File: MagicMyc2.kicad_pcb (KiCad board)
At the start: 2 copper layers, 43 x 31 mm, 32 parts, among them J1 RGB, J2 SPI, J3 PowerSupply, J4 Aout, J5 GPIOs, J6 PRG, J8 10102166A812A, Q1 BC338, U1 PIC18F15Q41-I/SS, U3 NCP1117-3.3_SOT223

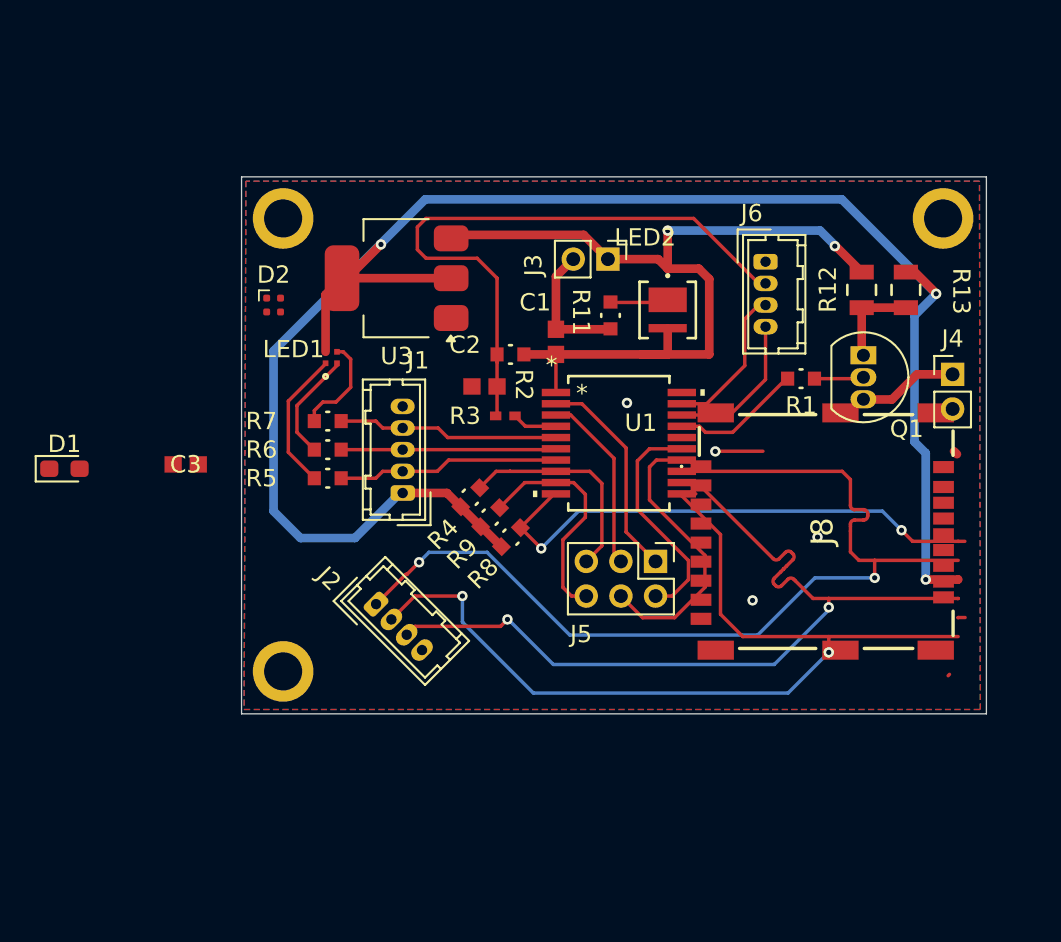
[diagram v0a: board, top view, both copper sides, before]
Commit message: v2: changed Pinout, Layout; removed 6V PG-LED
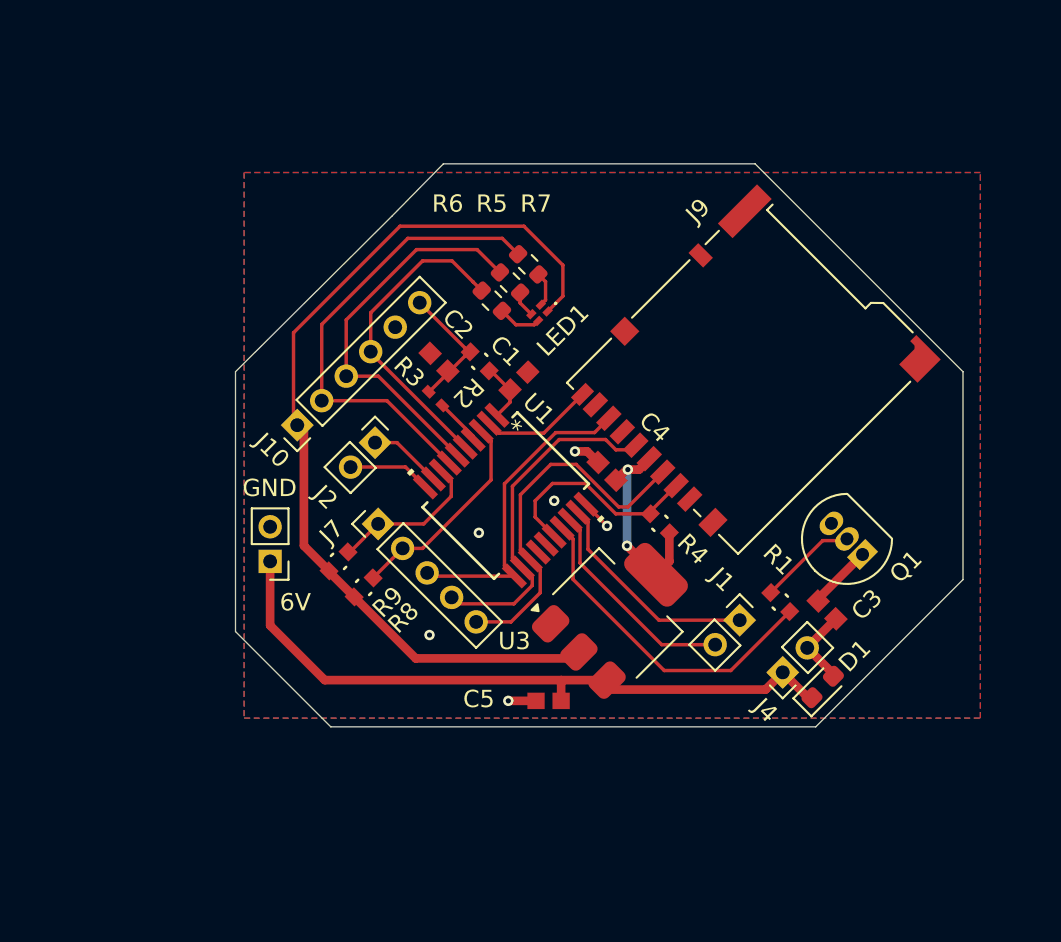
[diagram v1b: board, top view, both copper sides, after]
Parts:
- removed D2: ASMB-MTB1-0A3A2, LED_SMD:LED_Wurth_150044M155260
- removed J5: GPIOs, Connector_PinHeader_2.00mm:PinHeader_2x03_P2.00mm_Vertical
- removed J6: PRG, Connector_Hirose:Hirose_DF13-04P-1.25DSA_1x04_P1.25mm_Vertical
- removed J8: 10102166A812A, 10102166A812A:10102166A812A
- removed LED2: PG_6V, JB3030AWT-P-B65EA0000-N0000001:LED_J-SERIES_3030_CRW
- removed R11: 51 Ohm, RT0603DRE0710KL:RC0603N_YAG
- removed R12, R13: 0 Ohm, CRCW08050000Z0EA:RES_CRCW_0805_VIS
- removed REF** (x3): MountingHole_2.2mm_M2_ISO7380_Pad, MountingHole:MountingHole_2.2mm_M2_ISO7380_Pad
- added C4: 0.1 uF, C0603C103M5RAC7411:CAPC17595_87N_KEM, F.Cu at (76.0, 74.8)
- added C5: ? uF, C0603C103M5RAC7411:CAPC17595_87N_KEM, F.Cu at (72.6, 88.0)
- added J10: Conn_01x06, Connector_PinHeader_2.00mm:PinHeader_1x06_P2.00mm_Vertical, F.Cu at (58.1, 72.1)
- added J7: SPI_out, Connector_PinHeader_2.00mm:PinHeader_1x05_P2.00mm_Vertical, F.Cu at (62.7, 77.8)
- added J9: DM3BT-DSF-PEJS, Connector_Card:microSD_HC_Hirose_DM3BT-DSF-PEJS, F.Cu at (84.2, 69.0)
- J1: value RGB -> PowerSupply; footprint Connector_Hirose:Hirose_DF13-05P-1.25DSA_1x05_P1.25mm_Vertical -> Connector_PinHeader_2.00mm:PinHeader_1x02_P2.00mm_Vertical
- J2: value SPI -> PowerSupply; footprint Connector_Hirose:Hirose_DF13-04P-1.25DSA_1x04_P1.25mm_Vertical -> Connector_PinHeader_2.00mm:PinHeader_1x02_P2.00mm_Vertical
- LED1: value LED_RGB -> ASCB-HTC2-0A309; footprint UHD111A-FKA-C3K23E1L3VG5ZB3Z3:SMD4_UHD111A-FKA_CRW -> ASCB-HTC2-0A309:ASCBHTC20A309
- R5, R6, R7: value 51 Ohm -> 130; footprint RT0603DRE0710KL:RC0603N_YAG -> Resistor_SMD:R_0603_1608Metric
- moved D1 45.6 mm to (88.4, 87.2), turned to 45 degrees
- moved C3 38.0 mm to (88.7, 82.8), turned to 135 degrees
- moved J3 26.2 mm to (56.5, 80.0), turned to 180 degrees
- moved U3 23.2 mm to (76.5, 83.0), turned to 45 degrees
- moved J1 20.8 mm to (83.6, 83.3), turned to -45 degrees
- moved J4 19.8 mm to (86.1, 86.4), turned to 135 degrees
- moved R5 15.4 mm to (70.3, 63.9), turned to -45 degrees
- moved R7 14.7 mm to (71.4, 62.8), turned to 135 degrees
- moved R1 13.0 mm to (86.0, 82.3), turned to 135 degrees
- moved R6 12.8 mm to (69.3, 64.9), turned to 135 degrees
- moved LED1 12.3 mm to (72.0, 65.6), turned to 45 degrees
- moved Q1 11.5 mm to (90.7, 79.5), turned to 135 degrees
- moved R4 11.1 mm to (79.0, 77.8), turned to 135 degrees
- moved J2 9.32 mm to (62.6, 73.1)
- moved R9 9.12 mm to (60.5, 80.0)
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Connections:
- J1 pad 1: 3.3V -> ICSP_DATA
- J1 pad 2: LED_B -> ICSP_CLK
- J2 pad 1: SPI_MOSI -> RC7
- J2 pad 2: SPI_MISO -> RB7
- J4 pad 1: Aout -> Speaker_out
- J4 pad 2: GND -> Speaker_in 
- LED1 pad 1: Net-(LED1-Pad1) -> 3.3V
- LED1 pad 2: Net-(LED1-Pad2) -> Net-(LED1-CATHODE_BLUE)
- LED1 pad 3: Net-(LED1-Pad3) -> Net-(LED1-CATHODE_GREEN)
- LED1 pad 4: 3.3V -> Net-(LED1-CATHODE_RED)
- R4 pad 2: SPI_nCS3 -> SPI_nCS1
- R5 pad 1: unconnected-(R5-Pad1) -> LED_G
- R5 pad 2: LED_B -> Net-(LED1-CATHODE_GREEN)
- R6 pad 1: unconnected-(R6-Pad1) -> Net-(LED1-CATHODE_RED)
- R6 pad 2: LED_G -> LED_R
- R7 pad 1: LED_R -> Net-(LED1-CATHODE_BLUE)
- R7 pad 2: unconnected-(R7-Pad2) -> LED_B
- R8 pad 2: SPI_nCS1 -> SPI_nCS3
- U1 pad 10: SPI_nCS1 -> RB7
- U1 pad 16: unconnected-(U1-RC0-Pad16) -> SPI_nCS1
- U1 pad 2: RA5 -> SD_DETECT
- U1 pad 3: RA4 -> SPI_nCS3
- U1 pad 8: SPI_nCS3 -> SPI_nCS2
- U1 pad 9: SPI_nCS2 -> RC7
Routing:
- net VCC 6V: track 51.0 -> 0.00 mm
- net 3.3V: track 105.0 -> 65.4 mm, vias 3 -> 2
- net Speaker_out: track 0.00 -> 39.0 mm
- net SPI_MISO: track 53.8 -> 18.3 mm, vias 2 -> 0
- net SPI_MOSI: track 56.5 -> 21.3 mm, vias 2 -> 0
- net SPI_SCK: track 49.8 -> 20.0 mm, vias 2 -> 0
- net MCLR: track 36.7 -> 7.20 mm
- net SPI_nCS1: track 31.2 -> 12.5 mm, vias 2 -> 0
- net RC2: track 16.4 -> 0.00 mm
- net LED_B: track 12.8 -> 27.2 mm
- net RC1: track 13.2 -> 0.00 mm
- net RA5: track 12.4 -> 0.00 mm
- net DAC: track 7.49 -> 19.3 mm
- net RA4: track 10.5 -> 0.00 mm
- net LED_G: track 12.5 -> 22.8 mm
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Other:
- board size 43 x 31 mm -> 42 x 32.5 mm
- board text added: "6V"
- board text added: "GND"

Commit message: added drill holes back
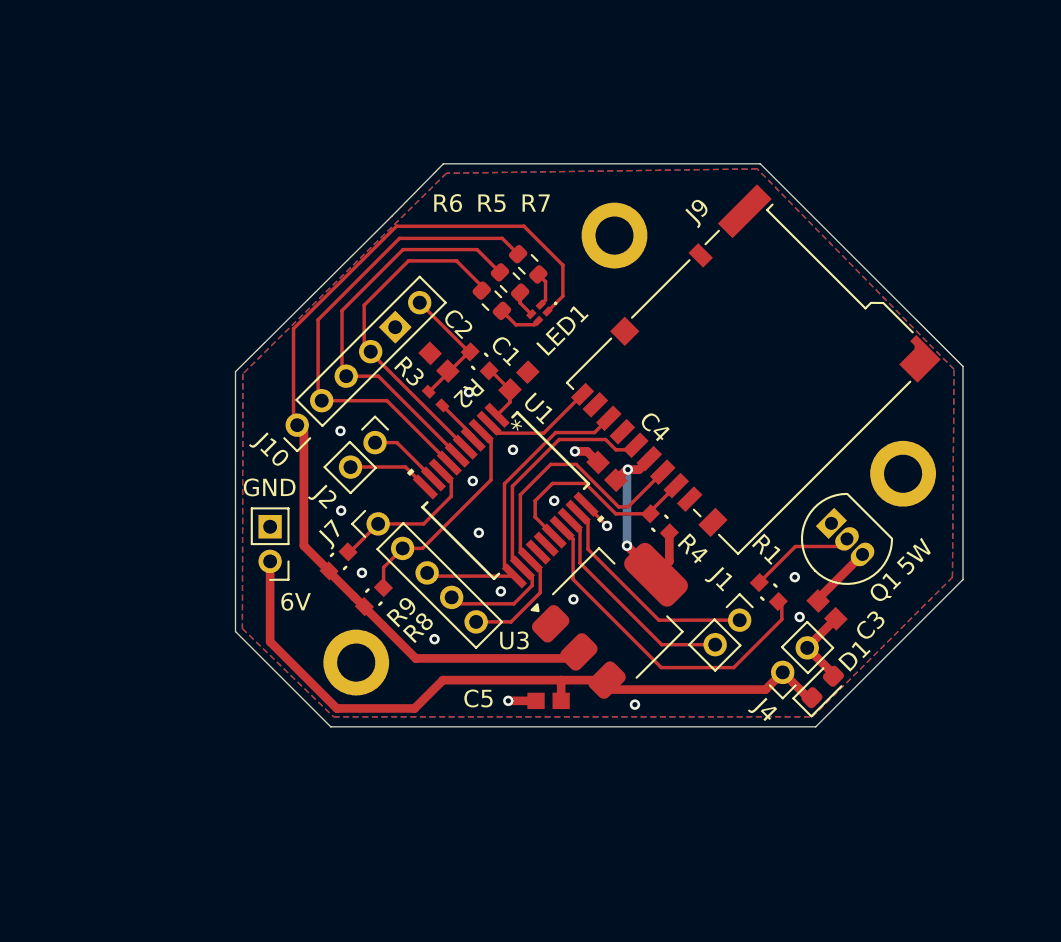
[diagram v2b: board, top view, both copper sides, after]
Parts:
- added REF**: MountingHole_2.2mm_M2_DIN965_Pad, MountingHole:MountingHole_2.2mm_M2_DIN965_Pad, F.Cu at (76.4, 61.1)
- added REF**: MountingHole_2.2mm_M2_DIN965_Pad, MountingHole:MountingHole_2.2mm_M2_DIN965_Pad, F.Cu at (93.0, 74.9)
- added REF**: MountingHole_2.2mm_M2_DIN965_Pad, MountingHole:MountingHole_2.2mm_M2_DIN965_Pad, F.Cu at (61.5, 85.8)
- moved R1 0.88 mm to (85.3, 81.7)
- moved R8 0.81 mm to (62.5, 82.0)
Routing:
- net Speaker_out: track 39.0 -> 40.9 mm
- net LED_R: track 18.4 -> 19.4 mm
- net LED_G: track 22.8 -> 23.4 mm
- net GND: track 4.95 -> 5.46 mm, vias 6 -> 17
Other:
- outline, holes or cut-outs redrawn
- board text added: "5W"

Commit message: Updated schematic pdf + some 3D models
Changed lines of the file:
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@@
 		(tags "CMS SOT")
 		(property "Reference" "U3"
-			(at -5.338656 -3.075914 0)
+			(at -5.444722 -3.082986 0)
 			(layer "F.SilkS")
 			(effects
@@
 			)
 		)
-		(model "S:/KiCad/Downloads/LIB_DM3BT-DSF-PEJS/DM3BT-DSF-PEJS/3D/DM3BT-DSF-PEJS.stl"
+		(model "${KICAD8_3DMODEL_DIR}/Connector_Card.3dshapes/microSD_HC_Hirose_DM3AT-SF-PEJM5.step"
 			(offset
 				(xyz 0 0 0)
@@
 		(tags "C0603C103M5RAC7411 ")
 		(property "Reference" "C2"
-			(at 0.777817 2.333452 -45)
+			(at 0.799031 2.411234 -45)
 			(unlocked yes)
 			(layer "F.SilkS")
@@
 		(tags "Through hole pin header THT 1x06 2.00mm single row")
 		(property "Reference" "J10"
-			(at 0 -2.06 135)
+			(at 0 -2.2832 135)
 			(layer "F.SilkS")
 			(effects
@@
 		(tags "Through hole pin header THT 1x02 2.00mm single row")
 		(property "Reference" "J4"
-			(at -0.848528 -2.252691 135)
+			(at -0.403051 -2.429468 0)
 			(layer "F.SilkS")
 			(effects
@@
 		(tags "LED")
 		(property "Reference" "LED1"
-			(at 0.247488 1.661702 45)
+			(at 0.98995 1.569778 -135)
 			(layer "F.SilkS")
 			(effects
@@
 		(tags "C0603C103M5RAC7411 ")
 		(property "Reference" "C1"
-			(at -0.689214 1.767767 -45)
+			(at -0.887204 1.45664 45)
 			(unlocked yes)
 			(layer "F.SilkS")
@@
 			)
 		)
+		(model "${KICAD8_3DMODEL_DIR}/Capacitor_SMD.3dshapes/C_01005_0402Metric.step"
+			(offset
+				(xyz 0 0 0)
+			)
+			(scale
+				(xyz 5 4 3)
+			)
+			(rotate
+				(xyz 0 0 0)
+			)
+		)
 	)
 	(footprint "Connector_PinHeader_2.00mm:PinHeader_1x02_P2.00mm_Vertical"
@@
 		(tags "to-92 sc-43 sc-43a sot54 PA33 transistor")
 		(property "Reference" "Q1"
-			(at -2.269813 -0.417193 45)
+			(at -2.2486 0.919239 45)
 			(layer "F.SilkS")
 			(effects
@@
 		(fp_arc
 			(start 0.3048 -3.7465)
-			(mid 0 -3.441698)
+			(mid 0 -3.441697)
 			(end -0.3048 -3.7465)
 			(stroke
@@
 			(font
 				(size 1 1)
-				(thickness 0.1)
+				(thickness 0.2)
+				(bold yes)
 			)
 			(justify left bottom)
@@
 	)
 	(gr_text "5W"
-		(at 94.15 80.13 45)
+		(at 93.93 78.61 0)
 		(layer "F.SilkS")
 		(effects
@@
 			(font
 				(size 1 1)
-				(thickness 0.1)
+				(thickness 0.2)
+				(bold yes)
 			)
 			(justify left bottom)

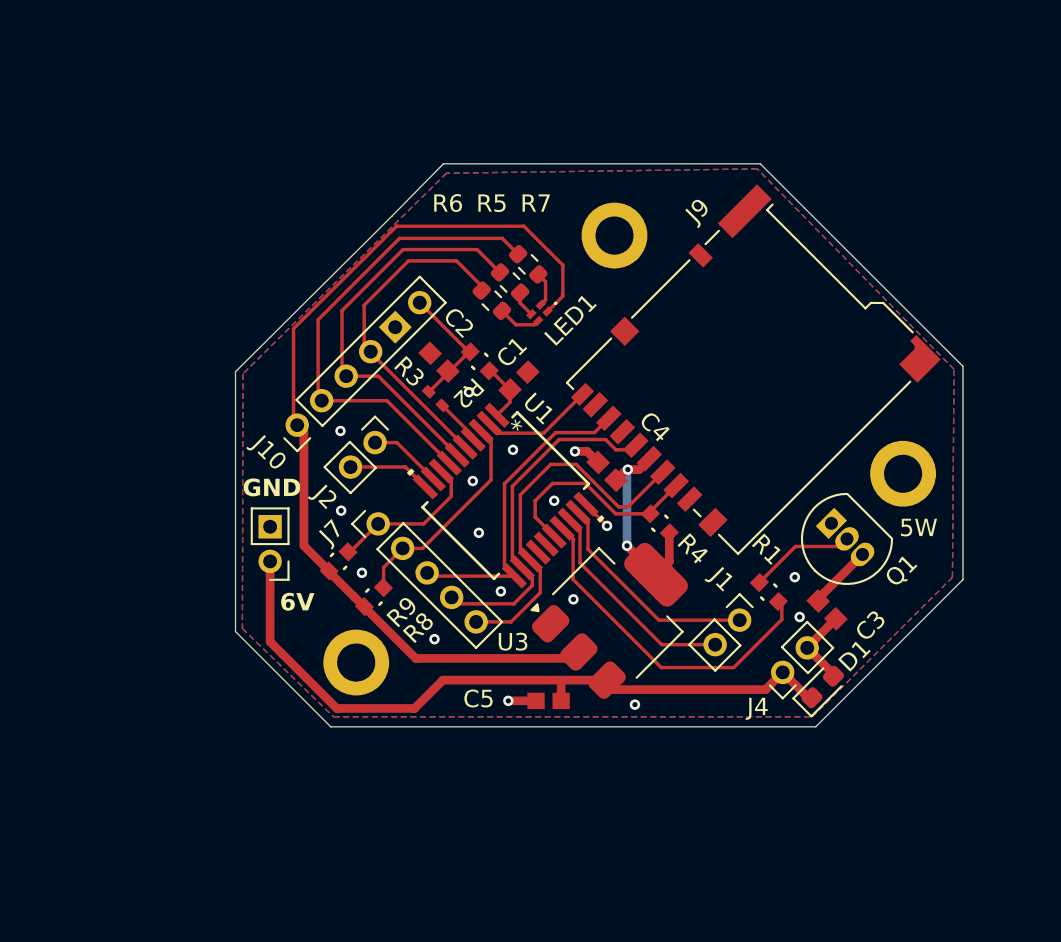
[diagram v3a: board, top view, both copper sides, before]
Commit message: Added design optimizations + Removed little ground islands by increasing min area size + Added teardrops + Fixes (almost) all errors + Added another 130Ohm resistor for RGB-LED (green) to maximize green power
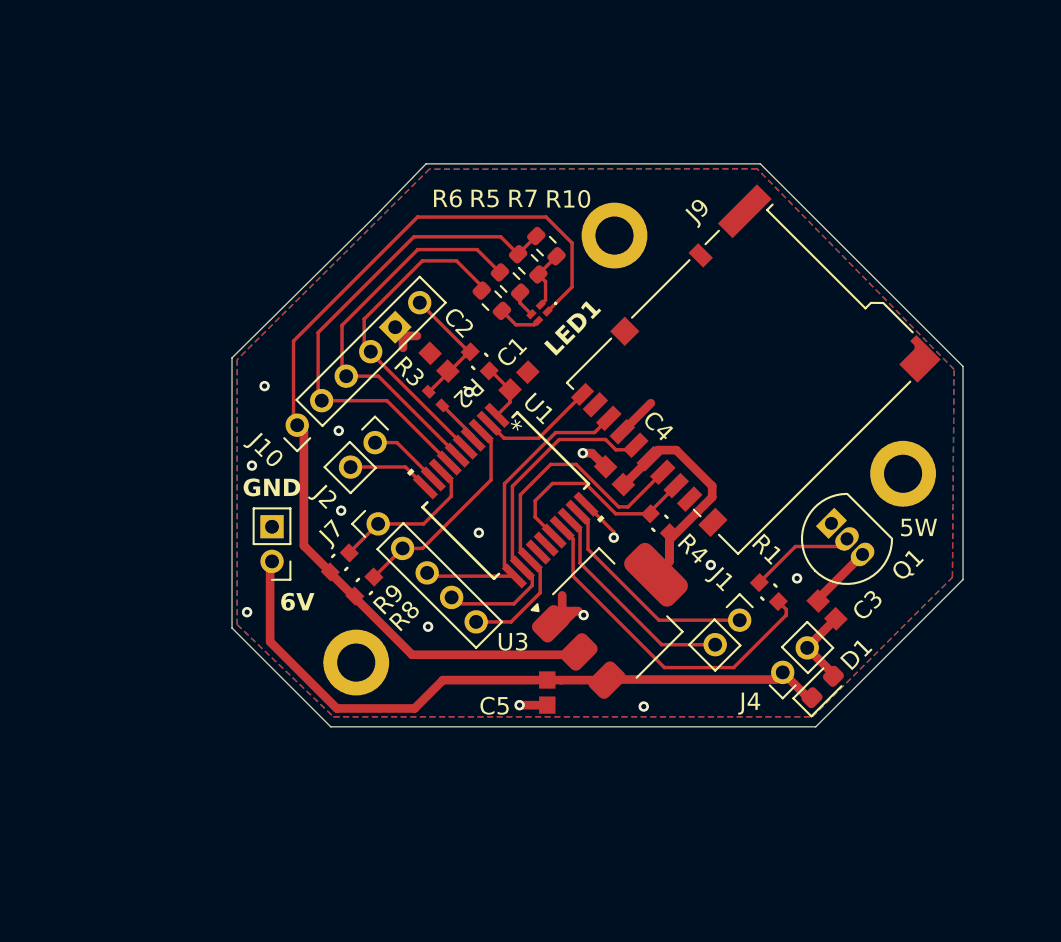
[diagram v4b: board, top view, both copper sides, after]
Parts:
- added R10: 130, Resistor_SMD:R_0603_1608Metric, F.Cu at (72.5, 61.8)
- moved R8 0.82 mm to (61.9, 81.4)
- moved C4 0.50 mm to (76.4, 75.0)
- moved C5 0.49 mm to (72.5, 87.5), turned to -90 degrees
- moved J3 0.11 mm to (56.6, 80.0)
- moved R9 0.09 mm to (60.5, 80.0)
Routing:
- net GND: track 5.46 -> 16.5 mm, vias 17 -> 15
- net 3.3V: track 65.6 -> 69.8 mm, vias 2 -> 0
- net Net-(LED1-CATHODE_BLUE): track 2.03 -> 3.52 mm
- net LED_B: track 27.7 -> 28.8 mm
- net Speaker_out: track 40.9 -> 39.8 mm
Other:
- board size 42 x 32.5 mm -> 42.2 x 32.5 mm

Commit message: Added rounded corners
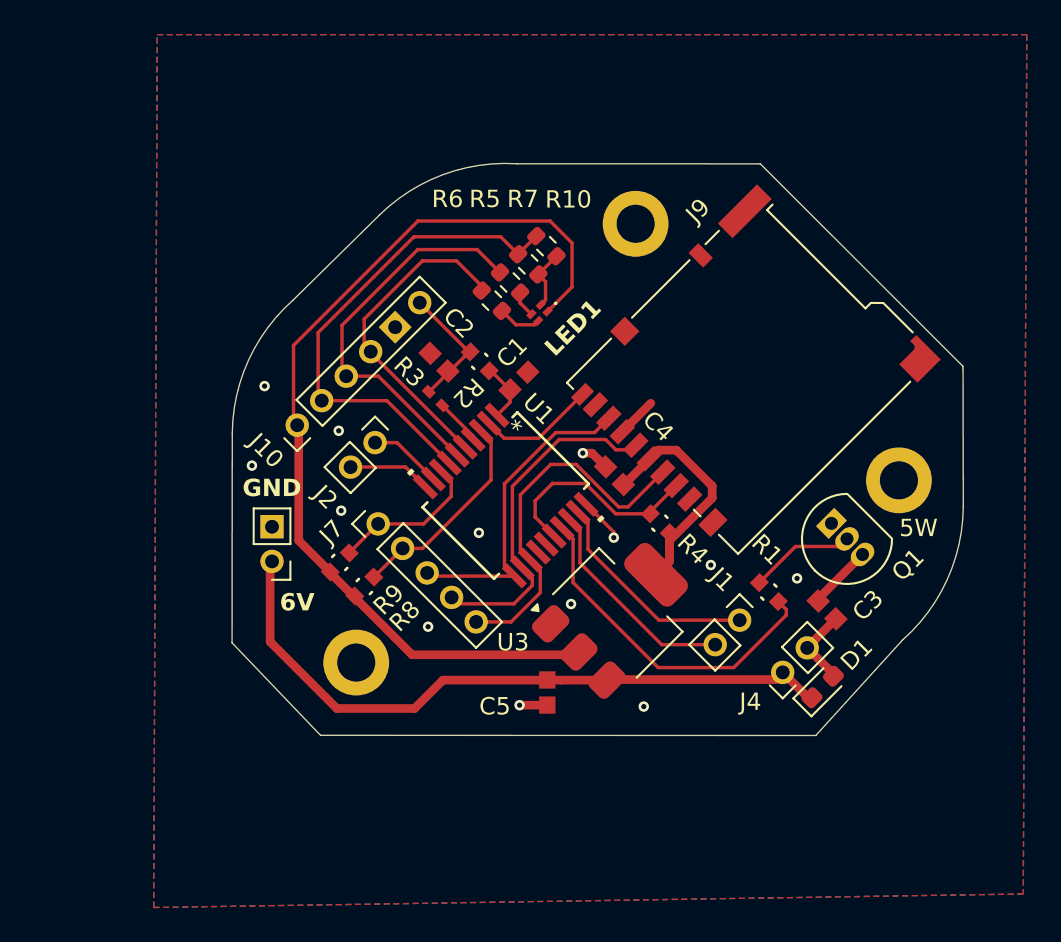
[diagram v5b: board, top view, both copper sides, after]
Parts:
- moved REF** 1.40 mm to (77.6, 60.5)
- moved REF** 0.45 mm to (92.8, 75.3)
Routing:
- net GND: track 16.5 -> 8.22 mm, vias 15 -> 13
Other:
- board size 42.2 x 32.5 mm -> 42.2 x 33 mm
